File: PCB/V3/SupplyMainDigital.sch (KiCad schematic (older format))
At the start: 94 parts, among them J1 IN, J2 3.3V, J3 OUT, J4 Conn_01x01, J5 Conn_01x01, J6 Conn_01x01, J7 Conn_01x01, P1 LEDs, P5 PGM, P6 SERIAL, P7 I2C, Q1 2N3904, Q2 2N3904, SW1 SW_PUSH, U1 TLC272, U12 TLC272, U2 MCP1501, U3 MCP1501, U4 MCP4922, U5 dsPIC33EPXXXGP502, U6 LT3081, U8 LM334Z, U9 MAX4080

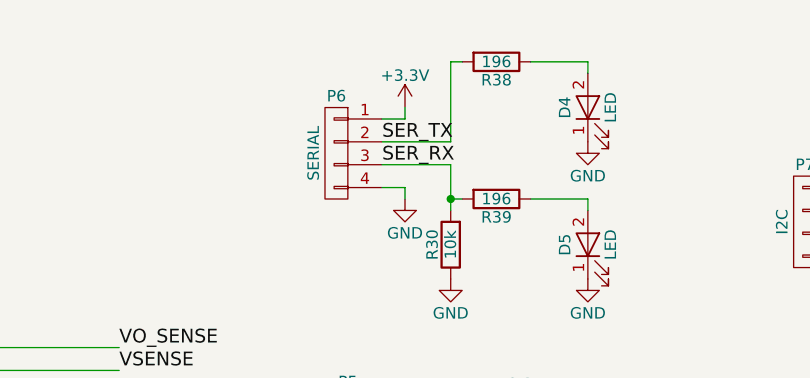
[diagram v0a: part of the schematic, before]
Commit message: first application + uart api
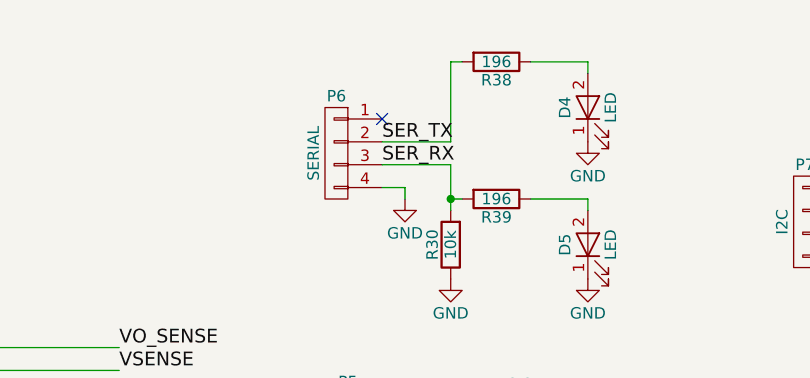
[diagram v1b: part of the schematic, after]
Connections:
- net +3V3: no longer P6.1 (P1)
- no-connect marks 9 -> 10
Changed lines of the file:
@@
-$EndComp
-$Comp
-L +3.3V #PWR013
-U 1 1 59365D86
-P 7950 900
-F 0 "#PWR013" H 7950 750 50  0001 C CNN
-F 1 "+3.3V" H 7950 1040 50  0000 C CNN
-F 2 "" H 7950 900 50  0000 C CNN
-F 3 "" H 7950 900 50  0000 C CNN
-	1    7950 900
-	1    0    0    -1
 $EndComp
 $Comp
@@
 	6050 3150 6250 3150
 Wire Wire Line
-	7850 950  7950 950
-Wire Wire Line
-	7950 950  7950 900
-Wire Wire Line
 	7850 1250 7950 1250
 Wire Wire Line
@@
 	14850 5900 14850 5850
 Connection ~ 14650 5900
+NoConn ~ 7850 950
 $EndSCHEMATC

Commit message: new software, reorden pcb layout
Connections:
- net VO_SENSE: no longer U12.1, U12.2 (-)
- new net: U12.1, U12.2 (-)
- no-connect marks 10 -> 9
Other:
- moved on the sheet: C10, C11, C12, C13, C14, C16, C21, C22, C23, C7, C9, D1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

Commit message: lcd pcb
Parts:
- C1, C10, C12, C15, C16, C2, C23: symbol CP -> SupplyMainDigital-rescue:CP
- C11, C13, C14, C21, C22, C3, C4, C5, C6, C7, C8, C9: symbol C -> SupplyMainDigital-rescue:C
- D1, D2, D4, D5, D6, D7: symbol LED -> SupplyMainDigital-rescue:LED
- D3: symbol D_Zener -> SupplyMainDigital-rescue:D_Zener
- HS1: symbol HEATSINK -> MyLib:HEATSINK
- J1, J3: symbol Barrel_Jack -> SupplyMainDigital-rescue:Barrel_Jack
- J2: symbol Conn_01x04 -> SupplyMainDigital-rescue:Conn_01x04
- J4, J5, J6, J7: symbol Conn_01x01 -> SupplyMainDigital-rescue:Conn_01x01
- JP3, JP5, JP6: symbol Jumper_NC_Small -> SupplyMainDigital-rescue:Jumper_NC_Small
- P1, P6, P7: symbol CONN_01X04 -> SupplyMainDigital-rescue:CONN_01X04
- P5: symbol CONN_01X05 -> SupplyMainDigital-rescue:CONN_01X05
- Q1, Q2: symbol 2N3904 -> SupplyMainDigital-rescue:2N3904
- R1, R10, R11, R12, R13, R14, R15, R16, R17, R18, R19, R2, R20, R21, R22, R23, R24, R25, R26, R27, R28, R29, R3, R30, R31, R32, R33, R34, R35, R36, R37, R38, R39, R4, R40, R41, R5, R6, R7, R8, R9: symbol R -> SupplyMainDigital-rescue:R
- SW1: symbol SW_PUSH -> SupplyMainDigital-rescue:SW_PUSH
- U1: symbol TLC272-RESCUE-SupplyMainDigital -> SupplyMainDigital-rescue:TLC272-RESCUE-SupplyMainDigital
- U12: symbol TLC272 -> SupplyMainDigital-rescue:TLC272
- U2, U3: symbol MCP1501 -> MyLib:MCP1501
- U4: symbol MCP4922 -> SupplyMainDigital-rescue:MCP4922
- U5: symbol dsPIC33EPXXXGP502 -> MyLib:dsPIC33EPXXXGP502
- U6: symbol LT3081 -> MyLib:LT3081
- U8: symbol LM334Z -> MyLib:LM334Z
- U9: symbol MAX4080 -> SupplyMainDigital-rescue:MAX4080

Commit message: added description and windows builds
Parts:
- HS1: symbol MyLib:HEATSINK -> SupplyMainDigital-rescue:HEATSINK-MyLib
- U2, U3: symbol MyLib:MCP1501 -> SupplyMainDigital-rescue:MCP1501-MyLib
- U5: symbol MyLib:dsPIC33EPXXXGP502 -> SupplyMainDigital-rescue:dsPIC33EPXXXGP502-MyLib
- U6: symbol MyLib:LT3081 -> SupplyMainDigital-rescue:LT3081-MyLib
- U8: symbol MyLib:LM334Z -> SupplyMainDigital-rescue:LM334Z-MyLib
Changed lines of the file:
@@
 $EndDescr
 $Comp
-L MyLib:dsPIC33EPXXXGP502 U5
+L SupplyMainDigital-rescue:dsPIC33EPXXXGP502-MyLib U5
 U 1 1 5932965F
 P 4750 3750
@@
 $EndComp
 $Comp
-L MyLib:LT3081 U6
+L SupplyMainDigital-rescue:LT3081-MyLib U6
 U 1 1 5932A3A1
 P 8100 3500
@@
 $EndComp
 $Comp
-L MyLib:MCP1501 U2
+L SupplyMainDigital-rescue:MCP1501-MyLib U2
 U 1 1 59330C43
 P 1300 3050
@@
 $EndComp
 $Comp
-L MyLib:MCP1501 U3
+L SupplyMainDigital-rescue:MCP1501-MyLib U3
 U 1 1 593355E9
 P 1300 4700
@@
 SPI_CS_DAC
 $Comp
-L MyLib:LM334Z U8
+L SupplyMainDigital-rescue:LM334Z-MyLib U8
 U 1 1 5934D471
 P 8800 4400
@@
 $EndComp
 $Comp
-L MyLib:HEATSINK HS1
+L SupplyMainDigital-rescue:HEATSINK-MyLib HS1
 U 1 1 5935704C
 P 8700 3150
